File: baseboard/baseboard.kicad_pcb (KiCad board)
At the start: 4 copper layers, 80 x 30 mm, 41 parts, among them J1 SWD, J2 USB_C_Receptacle_USB2.0_16P, J3 DISP, SW1 SW_Push, SW2 RST, U1 nRF52833-QDxx, U2 MCP1700x-330xxMB, X2 32kHz, Y1 32MHz

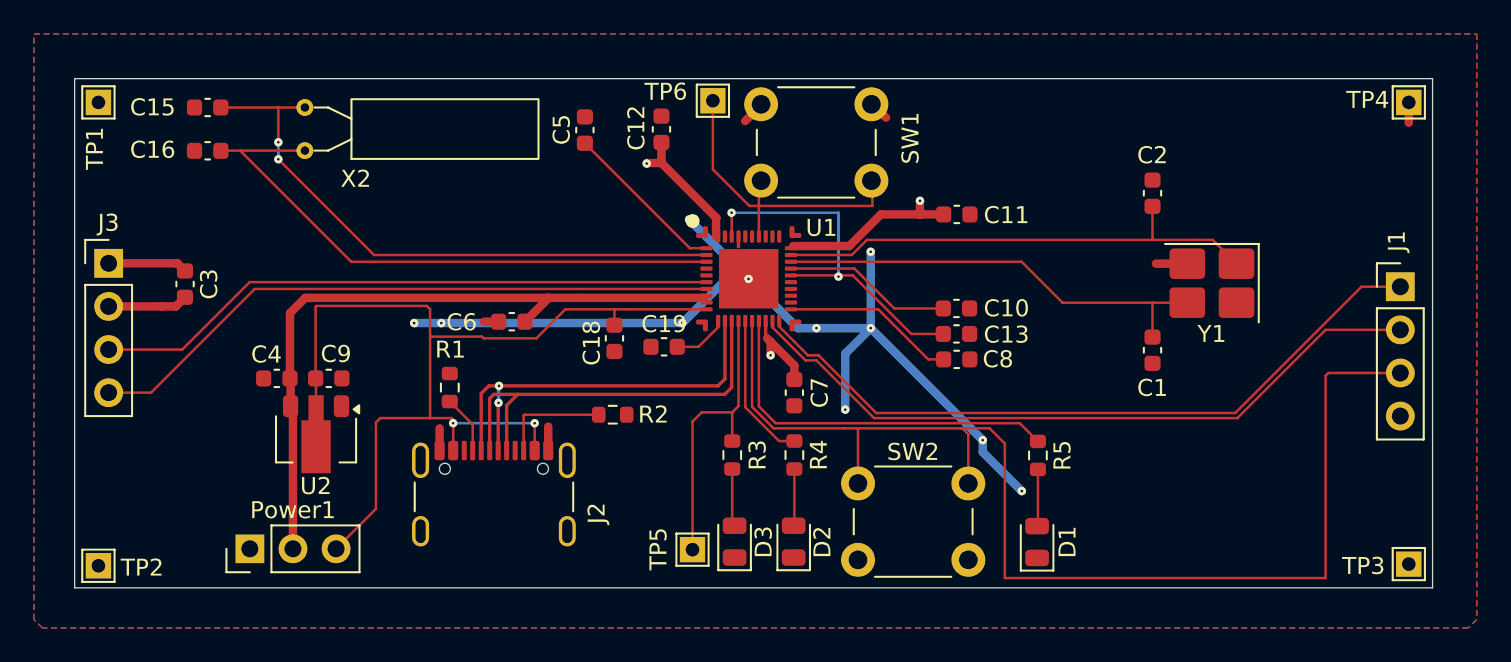
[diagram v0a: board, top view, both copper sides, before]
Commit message: Finished schematic & pcb design with extra components
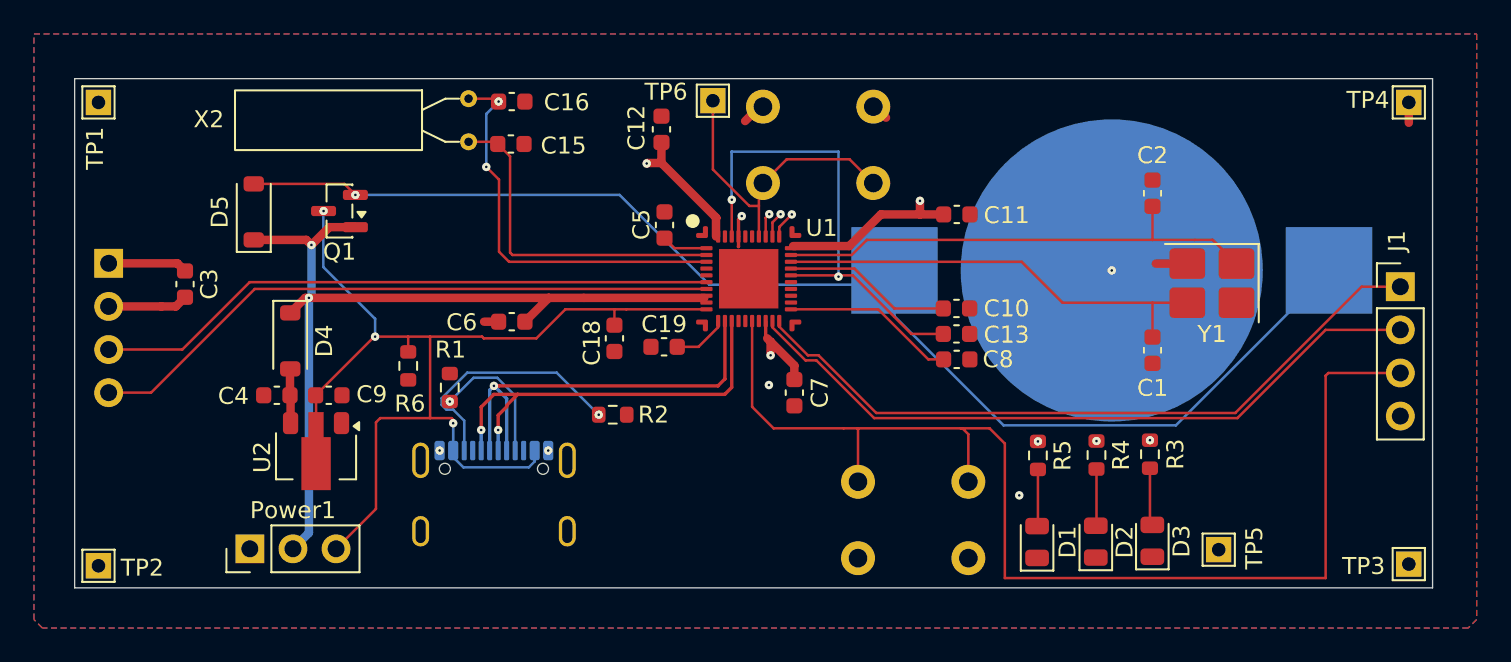
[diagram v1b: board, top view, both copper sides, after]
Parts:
- added BT1: Battery_Cell, Battery:BatteryHolder_Keystone_3002_1x2032, B.Cu at (161.1, 91.3)
- added D4: D_Schottky, Diode_SMD:D_SOD-123, F.Cu at (112.7, 95.5)
- added D5: D_Schottky, Diode_SMD:D_SOD-123, F.Cu at (110.5, 87.8)
- added Q1: Q_PMOS_DSG, Package_TO_SOT_SMD:SOT-23, F.Cu at (115.6, 87.8)
- added R6: 5.1kOhm, Resistor_SMD:R_0603_1608Metric, F.Cu at (119.7, 96.9)
- C4, C9: value 2.2µF -> 4.7µF
- J2, J3, SW1, SW2: moved to B.Cu
- moved TP5 31.0 mm to (167.4, 107.8)
- moved D3 24.6 mm to (163.5, 107.2)
- moved R3 24.6 mm to (163.3, 102.1)
- moved C16 18.1 mm to (125.8, 81.3), turned to 180 degrees
- moved C15 18.0 mm to (125.7, 83.8), turned to 180 degrees
- moved D2 17.8 mm to (160.2, 107.3)
- moved R4 17.8 mm to (160.2, 102.2)
- moved X2 10.1 mm to (123.2, 81.2), turned to -90 degrees
- moved C5 7.30 mm to (134.8, 88.6)
- moved SW1 6.61 mm to (147.1, 81.7), turned to 180 degrees
- moved SW2 6.50 mm to (146.2, 108.2), turned to 0 degrees
- moved C4 1.00 mm to (111.9, 98.7)
- moved C9 1.00 mm to (115.0, 98.7)
- moved U2 1.00 mm to (114.2, 102.2)
- turned J2 to 180 degrees
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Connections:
- C4 pad 1: +3.3V -> Net-(D4-A)
- U1 pad 14: /LED3 -> unconnected-(U1-P0.15-Pad14)
- U1 pad 15: /LED2 -> unconnected-(U1-P0.17-Pad15)
- U1 pad 17: /LED1 -> unconnected-(U1-P0.20-Pad17)
- U1 pad 31: unconnected-(U1-AIN1/P0.03-Pad31) -> /LED1
- U1 pad 32: unconnected-(U1-AIN0/P0.02-Pad32) -> /LED2
- U1 pad 33: unconnected-(U1-AIN4/P0.28-Pad33) -> /LED3
- U2 pad 3: +3.3V -> Net-(D4-A)
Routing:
- net Net-(BT1-+): track 0.00 -> 75.4 mm, vias 0 -> 1
- net GND: track 71.9 -> 13.1 mm, vias 11 -> 6
- net /LED3: track 17.3 -> 40.0 mm, vias 0 -> 2
- net /LED2: track 8.80 -> 26.0 mm, vias 0 -> 2
- net Net-(U1-P0.00/XL1): track 35.6 -> 20.1 mm, vias 2 -> 0
- net Net-(U1-P0.01/XL2): track 35.1 -> 23.8 mm, vias 0 -> 2
- net +3.3V: track 72.0 -> 83.0 mm, vias 3 -> 5
- net Net-(J2-CC2): track 7.08 -> 14.8 mm, vias 0 -> 1
- net /DEC4_6: track 21.9 -> 29.1 mm
- net Net-(U1-DEC1): track 9.72 -> 2.71 mm
- net +5V: track 58.6 -> 63.5 mm, vias 2 -> 3
- net Net-(J2-CC1): track 3.44 -> 8.10 mm, vias 0 -> 1
- net Net-(D4-A): track 0.00 -> 3.41 mm
- net /BUTTON1: track 19.2 -> 18.7 mm
- net /USBD+: track 25.1 -> 25.4 mm, vias 0 -> 2
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
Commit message: Fixed PCB and added an extra USB-A connector
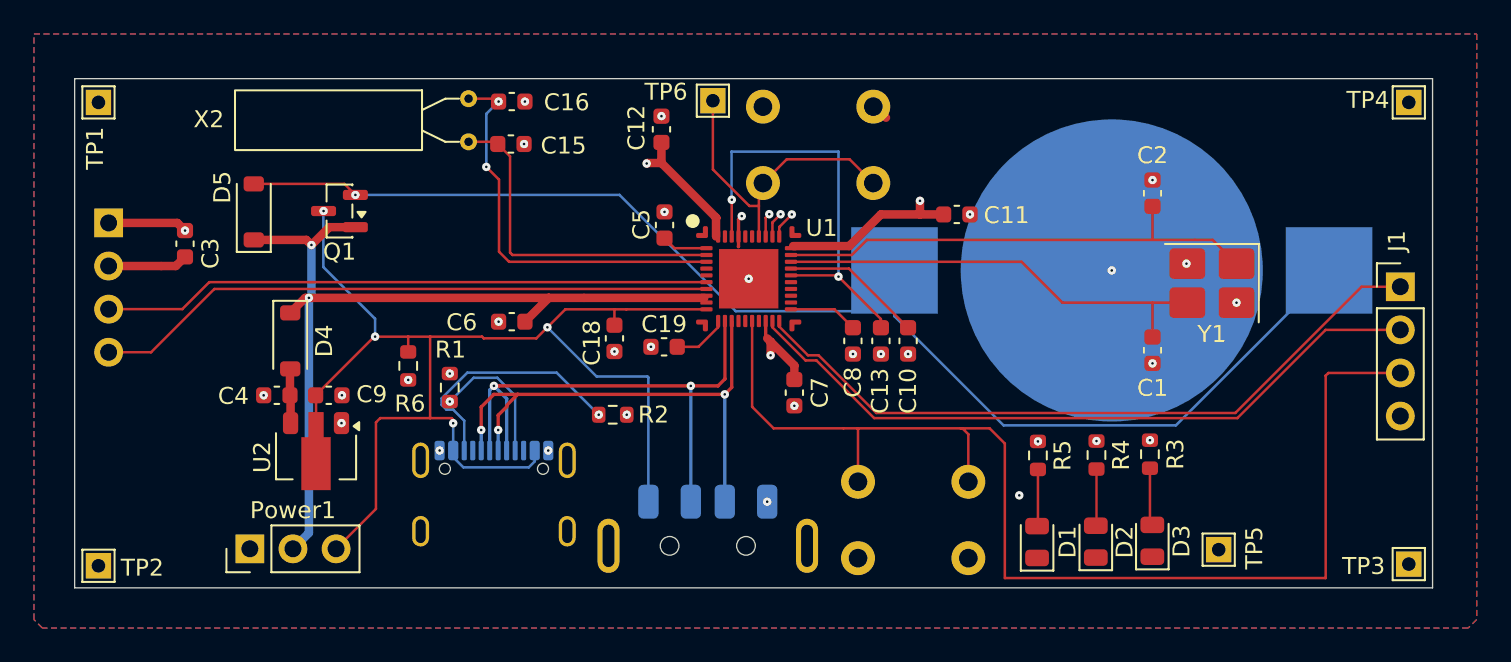
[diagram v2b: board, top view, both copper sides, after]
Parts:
- added J4: USB_A, Connector_USB:USB_A_Molex_48037-2200_Horizontal, B.Cu at (137.3, 115.9)
- SW1, SW2: footprint Button_Switch_THT:SW_PUSH_6mm_H9.5mm -> Button_Switch_THT:SW_PUSH_6mm
- moved C8 6.21 mm to (145.8, 95.5), turned to -90 degrees
- moved C13 4.47 mm to (147.5, 95.5), turned to 90 degrees
- moved C10 3.43 mm to (149.1, 95.5), turned to -90 degrees
- moved C3 2.38 mm to (106.5, 89.7)
- moved J3 2.38 mm to (102.0, 88.5)
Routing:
- net +5V: track 63.5 -> 78.0 mm, vias 3 -> 4
- net /USBD-: track 25.2 -> 32.0 mm, vias 1 -> 2
- net /USBD+: track 25.4 -> 31.8 mm, vias 2 -> 3
- net Net-(U1-DEC5): track 10.2 -> 4.10 mm
- net GND: track 13.1 -> 7.91 mm, vias 6 -> 30
- net /DEC4_6: track 29.1 -> 25.5 mm
- net Net-(U1-DEC3): track 9.95 -> 8.34 mm
- net Net-(BT1-+): track 75.4 -> 76.7 mm
- net Net-(J3-Pin_4): track 37.8 -> 36.8 mm
- net Net-(J3-Pin_3): track 36.9 -> 35.9 mm

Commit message: Fixed pcb & schematic
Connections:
- BT1 pad 2: GND -> +5V
- C1 pad 2: GND -> +5V
- C10 pad 2: GND -> +5V
- C11 pad 2: GND -> +5V
- C12 pad 2: GND -> +5V
- C13 pad 1: GND -> +5V
- C15 pad 1: GND -> +5V
- C16 pad 1: GND -> +5V
- C18 pad 2: GND -> +5V
- C19 pad 2: GND -> +5V
- C2 pad 2: GND -> +5V
- C3 pad 1: GND -> +5V
- C4 pad 2: GND -> +5V
- C5 pad 2: GND -> +5V
- C6 pad 2: GND -> +5V
- C7 pad 2: GND -> +5V
- C8 pad 2: GND -> +5V
- C9 pad 2: GND -> +5V
- D1 pad 1: GND -> +5V
- D2 pad 1: GND -> +5V
- D3 pad 1: GND -> +5V
- J1 pad 4: GND -> +5V
- J2 pad A1: GND -> +5V
- J2 pad A12: GND -> +5V
- J2 pad B1: GND -> +5V
- J2 pad B12: GND -> +5V
- J2 pad S1: GND -> +5V
- J3 pad 1: GND -> +5V
- J4 pad 4: GND -> +5V
- J4 pad 5: GND -> +5V
- Power1 pad 1: GND -> +5V
- R1 pad 1: GND -> +5V
- R2 pad 1: GND -> +5V
- R6 pad 2: GND -> +5V
- SW1 pad 1: GND -> +5V
- SW2 pad 1: GND -> +5V
- TP1 pad 1: GND -> +5V
- TP2 pad 1: GND -> +5V
- TP3 pad 1: GND -> +5V
- TP4 pad 1: GND -> +5V
- U1 pad 37: GND -> +5V
- U1 pad 41: GND -> +5V
- U2 pad 1: GND -> +5V
- Y1 pad 2: GND -> +5V
- Y1 pad 4: GND -> +5V
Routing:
- net +5V: track 78.0 -> 85.9 mm, vias 4 -> 34
- net GND: track 7.91 -> 0.00 mm, vias 30 -> 0
- net Net-(BT1-+): track 76.7 -> 79.1 mm
- added copper zone on B.Cu, net +5V
- added copper zone on F.Cu, net +5V
- removed copper zone on B.Cu, net GND
- removed copper zone on F.Cu, net GND

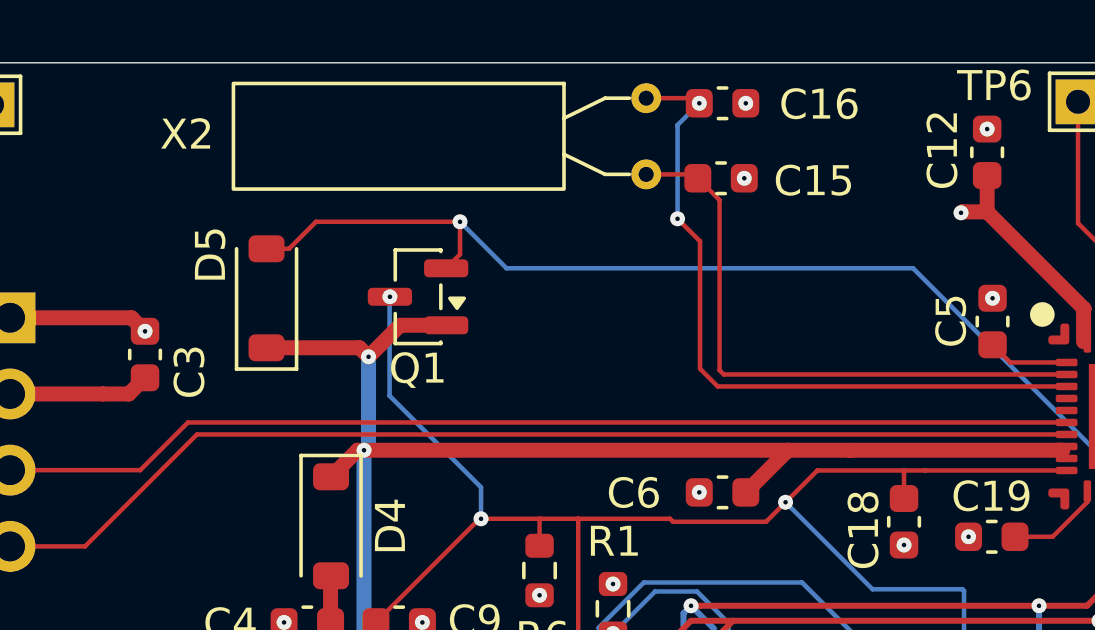
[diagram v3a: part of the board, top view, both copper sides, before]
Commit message: Fixed P-MOSFET and Schottky diode connected wrong on battery
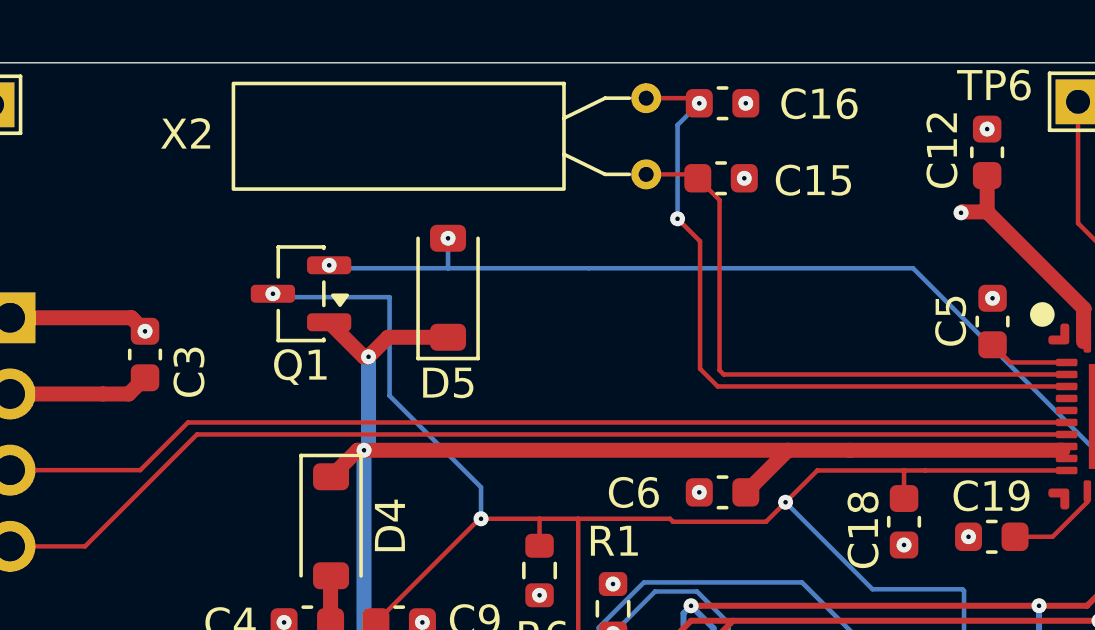
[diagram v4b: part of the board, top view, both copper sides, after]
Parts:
- moved D5 6.06 mm to (116.6, 87.5)
- moved Q1 3.90 mm to (111.7, 87.7)
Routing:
- net +5V: track 85.9 -> 89.8 mm
- net Net-(BT1-+): track 79.1 -> 75.3 mm, vias 1 -> 2
- net +3.3V: track 83.0 -> 81.1 mm
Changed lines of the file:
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@@
 	(footprint "Diode_SMD:D_SOD-123"
 		(layer "F.Cu")
-		(at 110.55 87.85 90)
+		(at 116.6 87.5 90)
 		(descr "SOD-123")
 		(tags "SOD-123")
 		(property "Reference" "D5"
-			(at 1.45 -1.85 90)
+			(at -3.2 0 180)
 			(layer "F.SilkS")
 			(effects
@@
 	(footprint "Package_TO_SOT_SMD:SOT-23"
 		(layer "F.Cu")
-		(at 115.6 87.8 180)
+		(at 111.7 87.7 180)
 		(descr "SOT, 3 Pin (JEDEC TO-236 Var AB https://www.jedec.org/document_search?search_api_views_fulltext=TO-236), generated with kicad-footprint-generator ipc_gullwing_generator.py")
 		(tags "SOT TO_SOT_SMD")
@@
 	)
 	(segment
-		(start 116.5375 88.75)
-		(end 115 88.75)
+		(start 149.8 88)
+		(end 149.8 87.2)
 		(width 0.5)
 		(layer "F.Cu")
@@
 	)
 	(segment
-		(start 149.8 88)
-		(end 149.8 87.2)
+		(start 113.8 92.916)
+		(end 127.929 92.916)
 		(width 0.5)
 		(layer "F.Cu")
@@
 	)
 	(segment
-		(start 113.8 92.916)
-		(end 127.929 92.916)
+		(start 113.95 89.8)
+		(end 113.7875 89.8)
 		(width 0.5)
 		(layer "F.Cu")
@@
 	)
 	(segment
+		(start 113.7875 89.8)
+		(end 112.6375 88.65)
+		(width 0.5)
+		(layer "F.Cu")
+		(net 3)
+	)
+	(segment
 		(start 140.71 95.21)
 		(end 140.8 95.3)
@@
 	)
 	(segment
-		(start 110.55 89.5)
-		(end 113.65 89.5)
-		(width 0.5)
-		(layer "F.Cu")
-		(net 3)
-	)
-	(segment
 		(start 137.784 88.216)
 		(end 137.784 89.3)
@@
 	)
 	(segment
-		(start 113.65 89.5)
-		(end 113.95 89.8)
-		(width 0.5)
-		(layer "F.Cu")
-		(net 3)
-	)
-	(segment
 		(start 134.57 84.97)
 		(end 137.8 88.2)
@@
 	)
 	(segment
-		(start 115 88.75)
-		(end 113.95 89.8)
+		(start 102 91.04)
+		(end 105.1 91.04)
 		(width 0.5)
 		(layer "F.Cu")
@@
 	)
 	(segment
-		(start 102 91.04)
-		(end 105.1 91.04)
+		(start 151.195 88)
+		(end 149.8 88)
 		(width 0.5)
 		(layer "F.Cu")
@@
 	)
 	(segment
-		(start 151.195 88)
-		(end 149.8 88)
+		(start 114.6 89.15)
+		(end 116.6 89.15)
 		(width 0.5)
 		(layer "F.Cu")
@@
 	)
 	(segment
+		(start 113.95 89.8)
+		(end 114.6 89.15)
+		(width 0.5)
+		(layer "F.Cu")
+		(net 3)
+	)
+	(segment
 		(start 112.72 107.77)
 		(end 112.75 107.8)
@@
 	)
 	(via
-		(at 114.6625 87.8)
+		(at 121.5 101.91)
 		(size 0.5)
 		(drill 0.15)
@@
 	)
 	(via
-		(at 121.5 101.91)
+		(at 142.4 99.275)
 		(size 0.5)
 		(drill 0.15)
@@
 	)
 	(via
-		(at 142.4 99.275)
+		(at 110.7625 87.7)
 		(size 0.5)
 		(drill 0.15)
@@
 	)
 	(segment
-		(start 126.754347 102.9)
-		(end 127.1 102.554347)
+		(start 110.875 87.8125)
+		(end 110.7625 87.7)
 		(width 0.15)
 		(layer "B.Cu")
@@
 	)
 	(segment
-		(start 117.7 94.15)
-		(end 114.65 91.1)
+		(start 126.754347 102.9)
+		(end 127.1 102.554347)
 		(width 0.15)
 		(layer "B.Cu")
@@
 	)
 	(segment
-		(start 114.65 87.8125)
-		(end 114.6625 87.8)
+		(start 114.65 91.1)
+		(end 114.65 87.8125)
 		(width 0.15)
 		(layer "B.Cu")
@@
 	)
 	(segment
-		(start 114.65 91.1)
-		(end 114.65 87.8125)
+		(start 117.7 94.15)
+		(end 114.65 91.1)
 		(width 0.15)
 		(layer "B.Cu")
@@
 	)
 	(segment
+		(start 114.65 87.8125)
+		(end 110.875 87.8125)
+		(width 0.15)
+		(layer "B.Cu")
+		(net 6)
+	)
+	(segment
 		(start 122.9 102.9)
 		(end 126.754347 102.9)
@@
 		(net 29)
 	)
-	(segment
-		(start 117 85.3)
-		(end 117 86.3875)
-		(width 0.15)
-		(layer "F.Cu")
-		(net 39)
-	)
-	(segment
-		(start 112.2 85.3)
-		(end 111.3 86.2)
-		(width 0.15)
-		(layer "F.Cu")
-		(net 39)
-	)
-	(segment
-		(start 111.3 86.2)
-		(end 110.55 86.2)
-		(width 0.15)
-		(layer "F.Cu")
-		(net 39)
-	)
-	(segment
-		(start 117 85.3)
-		(end 112.2 85.3)
-		(width 0.15)
-		(layer "F.Cu")
-		(net 39)
-	)
-	(segment
-		(start 117 86.3875)
-		(end 116.5375 86.85)
-		(width 0.15)
-		(layer "F.Cu")
+	(via
+		(at 112.6375 86.75)
+		(size 0.5)
+		(drill 0.15)
+		(layers "F.Cu" "B.Cu")
 		(net 39)
 	)
 	(via
-		(at 117 85.3)
+		(at 116.6 85.85)
 		(size 0.5)
 		(drill 0.15)
@@
 	)
 	(segment
+		(start 121.3 86.85)
+		(end 116.6 86.85)
+		(width 0.15)
+		(layer "B.Cu")
+		(net 39)
+	)
+	(segment
 		(start 173.9 91.3)
 		(end 173.9 91.406113)
@@
 	)
 	(segment
-		(start 118.55 86.85)
+		(start 121.3 86.85)
 		(end 132.1 86.85)
 		(width 0.15)
@@
 	)
 	(segment
+		(start 116.6 86.85)
+		(end 112.7375 86.85)
+		(width 0.15)
+		(layer "B.Cu")
+		(net 39)
+	)
+	(segment
 		(start 145.9 93.7)
 		(end 148.3 91.3)
@@
 	)
 	(segment
-		(start 117 85.3)
-		(end 118.55 86.85)
+		(start 112.7375 86.85)
+		(end 112.6375 86.75)
 		(width 0.15)
 		(layer "B.Cu")
@@
 		(width 0.15)
 		(layer "B.Cu")
+		(net 39)
+	)
+	(segment
+		(start 116.6 86.85)
+		(end 116.6 85.85)
+		(width 0.15)
+		(layer "B.Cu")
